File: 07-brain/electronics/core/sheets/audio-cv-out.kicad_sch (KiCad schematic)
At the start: 19 parts, among them U6 MCP6002-xSN, U7 CD4053B, U8 MCP4822

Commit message: Brain schematics WIP
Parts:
- removed C11, C12: 100n, Capacitor_SMD:C_0603_1608Metric, symbol Device:C
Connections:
- net AUDIO_CV_OUT_1: no longer R31.2, R32.2
- net GND renamed GNDA
- net OUT_1_SWITCH renamed OUT_SWITCH_S1
- net OUT_2_SWITCH renamed OUT_SWITCH_S2
- new net AUDIO_CV_OUT_2: R31.2, R32.2
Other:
- note added: "Should I put a resistor on each output of the switch so that the signal can't go back to the switch?"
- moved on the sheet: C13, C14

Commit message: Updated Brain schematics
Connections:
- net OUT_SWITCH_S1 renamed OUT_COUPLING_S1
- net OUT_SWITCH_S2 renamed OUT_COUPLING_S2
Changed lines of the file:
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@@
 		)
 	)
-	(hierarchical_label "OUT_SWITCH_S2"
+	(hierarchical_label "OUT_COUPLING_S2"
 		(shape input)
 		(at 109.22 50.8 180)
@@
 		)
 	)
-	(hierarchical_label "OUT_SWITCH_S1"
+	(hierarchical_label "OUT_COUPLING_S1"
 		(shape input)
 		(at 109.22 48.26 180)

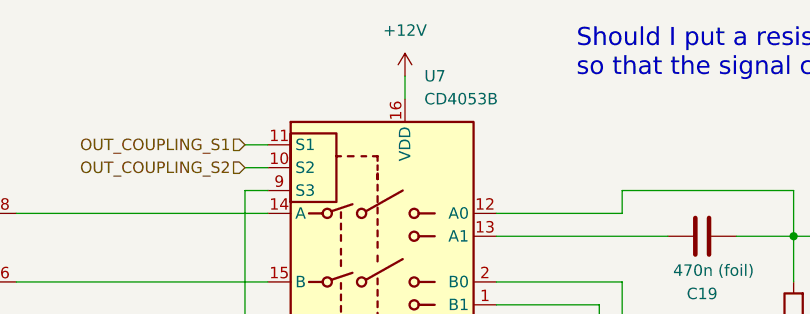
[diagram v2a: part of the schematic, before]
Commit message: Added AudioCVOut class to BrainSDK (untested)
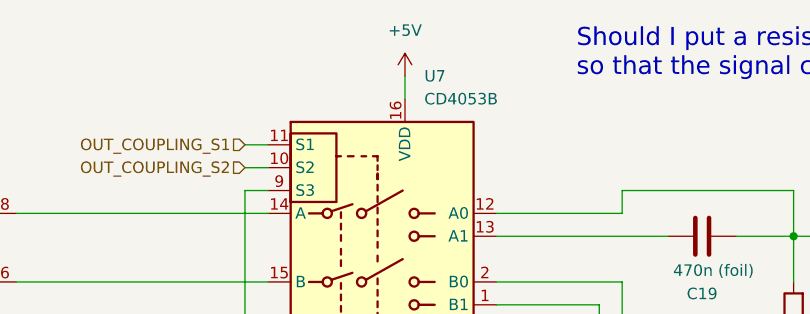
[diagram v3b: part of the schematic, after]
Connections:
- net +12V: no longer U7.16 (VDD)
- net +5V: now also U7.16 (VDD)
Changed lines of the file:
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@@
-	)
-	(symbol
-		(lib_name "+12V_2")
-		(lib_id "power:+12V")
-		(at 127 40.64 0)
-		(unit 1)
-		(exclude_from_sim no)
-		(in_bom yes)
-		(on_board yes)
-		(dnp no)
-		(fields_autoplaced yes)
-		(property "Reference" "#PWR047"
-			(at 127 44.45 0)
-			(effects
-				(font
-					(size 1.27 1.27)
-				)
-				(hide yes)
-			)
-		)
-		(property "Value" "+12V"
-			(at 127 35.56 0)
-			(effects
-				(font
-					(size 1.27 1.27)
-				)
-			)
-		)
-		(property "Footprint" ""
-			(at 127 40.64 0)
-			(effects
-				(font
-					(size 1.27 1.27)
-				)
-				(hide yes)
-			)
-		)
-		(property "Datasheet" ""
-			(at 127 40.64 0)
-			(effects
-				(font
-					(size 1.27 1.27)
-				)
-				(hide yes)
-			)
-		)
-		(property "Description" ""
-			(at 127 40.64 0)
-			(effects
-				(font
-					(size 1.27 1.27)
-				)
-				(hide yes)
-			)
-		)
-		(pin "1"
-		)
-		(instances
-			(project "brain-core"
-				(path "/8e2e31f3-eed5-4de1-966c-f4162758c735/a5dac03c-0548-4574-b19b-4dd5fbd38e47"
-					(reference "#PWR047")
-					(unit 1)
-				)
-			)
-		)
 	)
 	(symbol
@@
 					(unit 1)
 				)
+			)
+		)
+	)
+	(symbol
+		(lib_name "+5V_1")
+		(lib_id "power:+5V")
+		(at 127 40.64 0)
+		(unit 1)
+		(exclude_from_sim no)
+		(in_bom yes)
+		(on_board yes)
+		(dnp no)
+		(fields_autoplaced yes)
+		(property "Reference" "#PWR030"
+			(at 127 44.45 0)
+			(effects
+				(font
+					(size 1.27 1.27)
+				)
+				(hide yes)
+			)
+		)
+		(property "Value" "+5V"
+			(at 127 35.56 0)
+			(effects
+				(font
+					(size 1.27 1.27)
+				)
+			)
+		)
+		(property "Footprint" ""
+			(at 127 40.64 0)
+			(effects
+				(font
+					(size 1.27 1.27)
+				)
+				(hide yes)
+			)
+		)
+		(property "Datasheet" ""
+			(at 127 40.64 0)
+			(effects
+				(font
+					(size 1.27 1.27)
+				)
+				(hide yes)
+			)
+		)
+		(property "Description" "Power symbol creates a global label with name \"+5V\""
+			(at 127 40.64 0)
+			(effects
+				(font
+					(size 1.27 1.27)
+				)
+				(hide yes)
+			)
+		)
+		(pin "1"
+		)
+		(instances
+			(project "brain-core"
+				(path "/8e2e31f3-eed5-4de1-966c-f4162758c735/a5dac03c-0548-4574-b19b-4dd5fbd38e47"
+					(reference "#PWR030")
+					(unit 1)
+				)

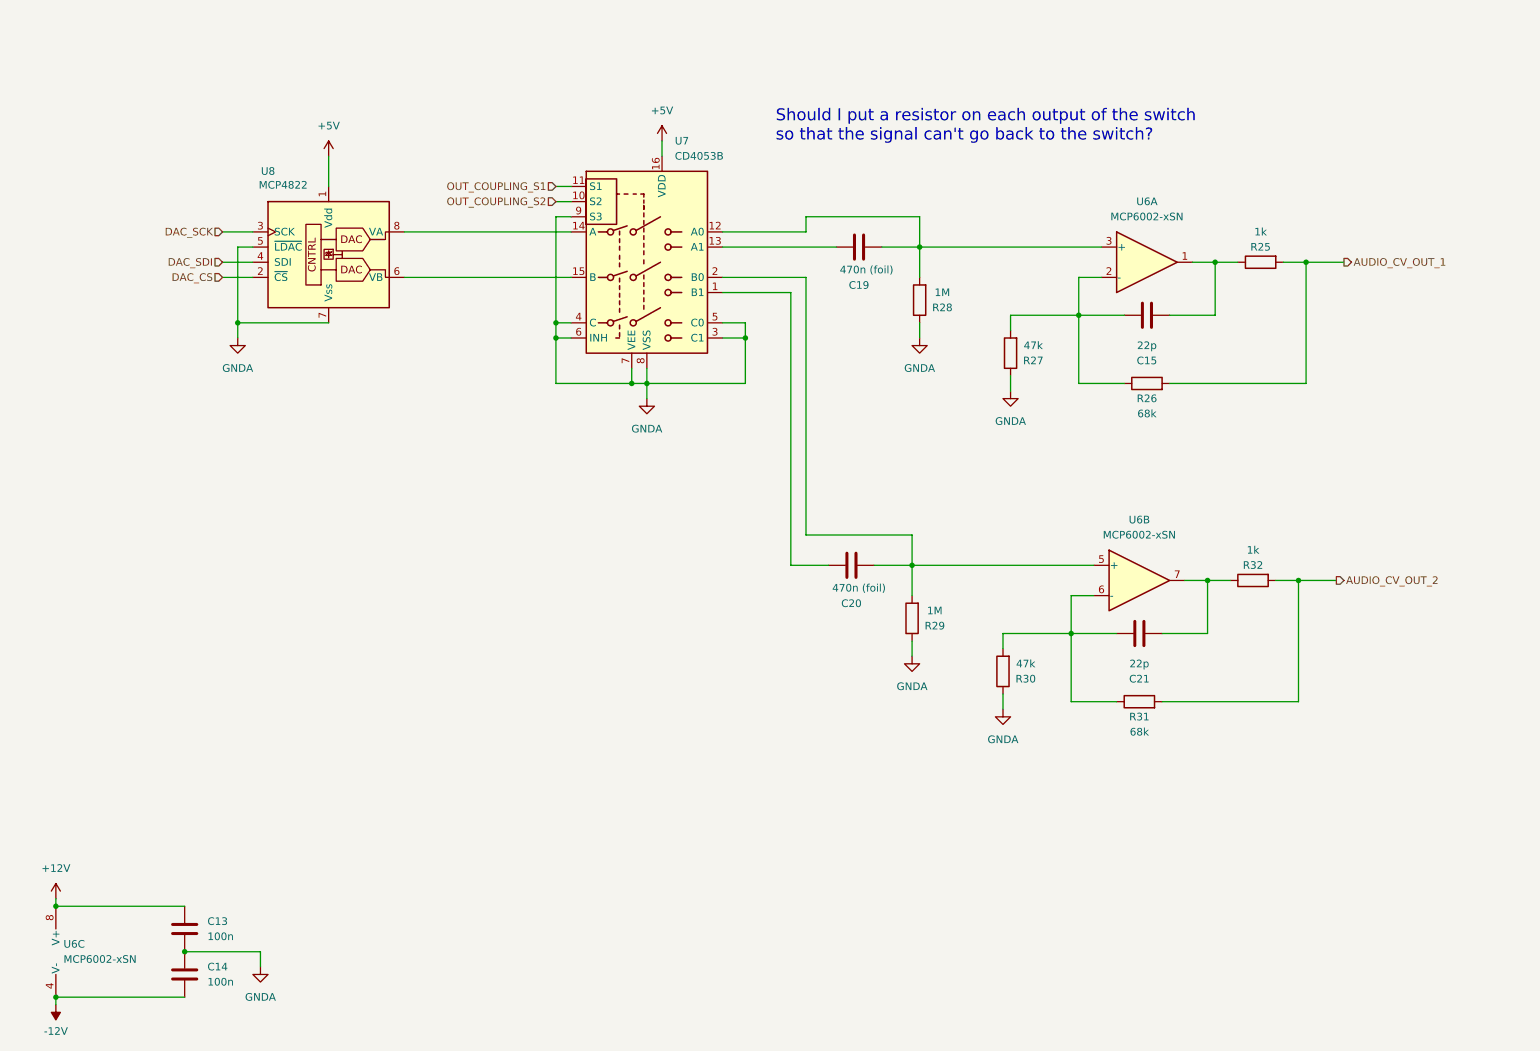
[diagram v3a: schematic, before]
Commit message: Genius level shifter in Brain output
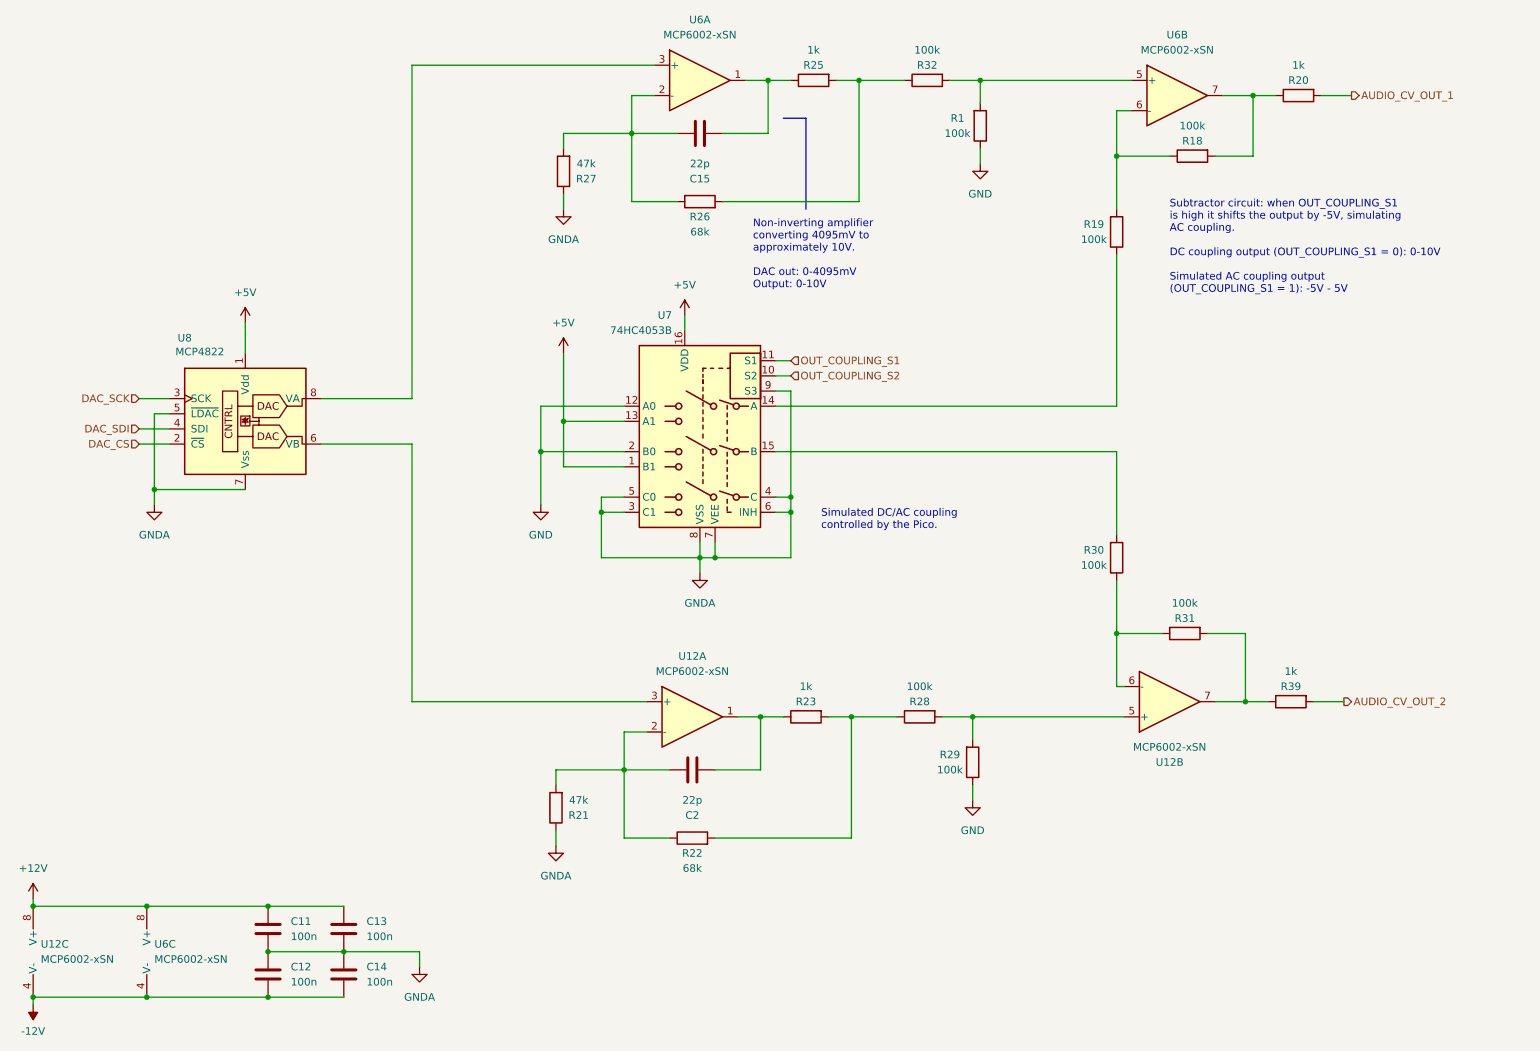
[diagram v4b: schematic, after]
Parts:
- removed C19, C20: 470n (foil), Capacitor_THT:C_Rect_L7.0mm_W3.5mm_P5.00mm, symbol Device:C
- removed C21: 22p, Capacitor_SMD:C_0603_1608Metric, symbol Device:C
- added C11, C12: 100n, Capacitor_SMD:C_0603_1608Metric, symbol Device:C
- added C2: 22p, Capacitor_SMD:C_0603_1608Metric, symbol Device:C
- added R1, R18, R19: 100k, Resistor_SMD:R_0603_1608Metric, symbol Device:R
- added R20, R23, R39: 1k, Resistor_SMD:R_0603_1608Metric, symbol Device:R
- added R21: 47k, Resistor_SMD:R_0603_1608Metric, symbol Device:R
- added R22: 68k, Resistor_SMD:R_0603_1608Metric, symbol Device:R
- added U12: MCP6002-xSN, symbol Amplifier_Operational:MCP6002-xSN
- R28, R29: value 1M -> 100k
- R30: value 47k -> 100k
- R31: value 68k -> 100k
- R32: value 1k -> 100k
- U7: value CD4053B -> 74HC4053B
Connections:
- net +12V: now also C11.1, U12.8 (V+)
- net +5V: now also U7.1 (B1), U7.13 (A1)
- net -12V: now also C12.2, U12.4 (V-)
- net AUDIO_CV_OUT_1: now also R20.2; no longer R25.2, R26.2
- net AUDIO_CV_OUT_2: now also R39.2; no longer R31.2, R32.2
- net GNDA: now also C11.2, C12.1, R21.1; no longer R28.1, R29.1, R30.1
- net at R32.1: now also R25.2, R26.2; no longer U6.7
- net at U8.6 (VB): now also U12.3 (+); no longer U7.15 (B)
- net at U7.14 (A): now also R19.1; no longer U8.8 (VA)
- new net: R18.1, R19.2, U6.6 (-)
- new net: R28.2, R29.2, U12.5 (+)
- new net: R1.2, R32.2, U6.5 (+)
- new net: U6.3 (+), U8.8 (VA)
- new net: C2.2, R23.1, U12.1
- new net: R22.2, R23.2, R28.1
- new net: R31.2, R39.1, U12.7
- new net: C2.1, R21.2, R22.1, U12.2 (-)
- new net: R30.1, R31.1, U12.6 (-)
- new net: R30.2, U7.15 (B)
- new net: R18.2, R20.1, U6.7
- new net GND: R1.1, R29.1, U7.12 (A0), U7.2 (B0)
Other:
- note added: "Non-inverting amplifier converting 4095mV to approximately 10V. DAC out: 0-4095mV Output: 0-10V"
- note added: "Simulated DC/AC coupling controlled by the Pico."
- note added: "Subtractor circuit: when OUT_COUPLING_S1 is high it shifts the output by -5V, simulating AC coupling. DC coupling output (OUT_COUPLING_S1 = 0): 0-10V Simulated AC coupling output (OUT_COUPLING_S1 = 1): -5V - 5V"
- note removed: "Should I put a resistor on each output of the switch so that the signal can't go back to the switch?"
- moved on the sheet: C13, C14, C15, R25, R26, R27, R32, U6A, U6B, U6C, U7, U8

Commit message: Audio/CV out BrainSDK tested/working
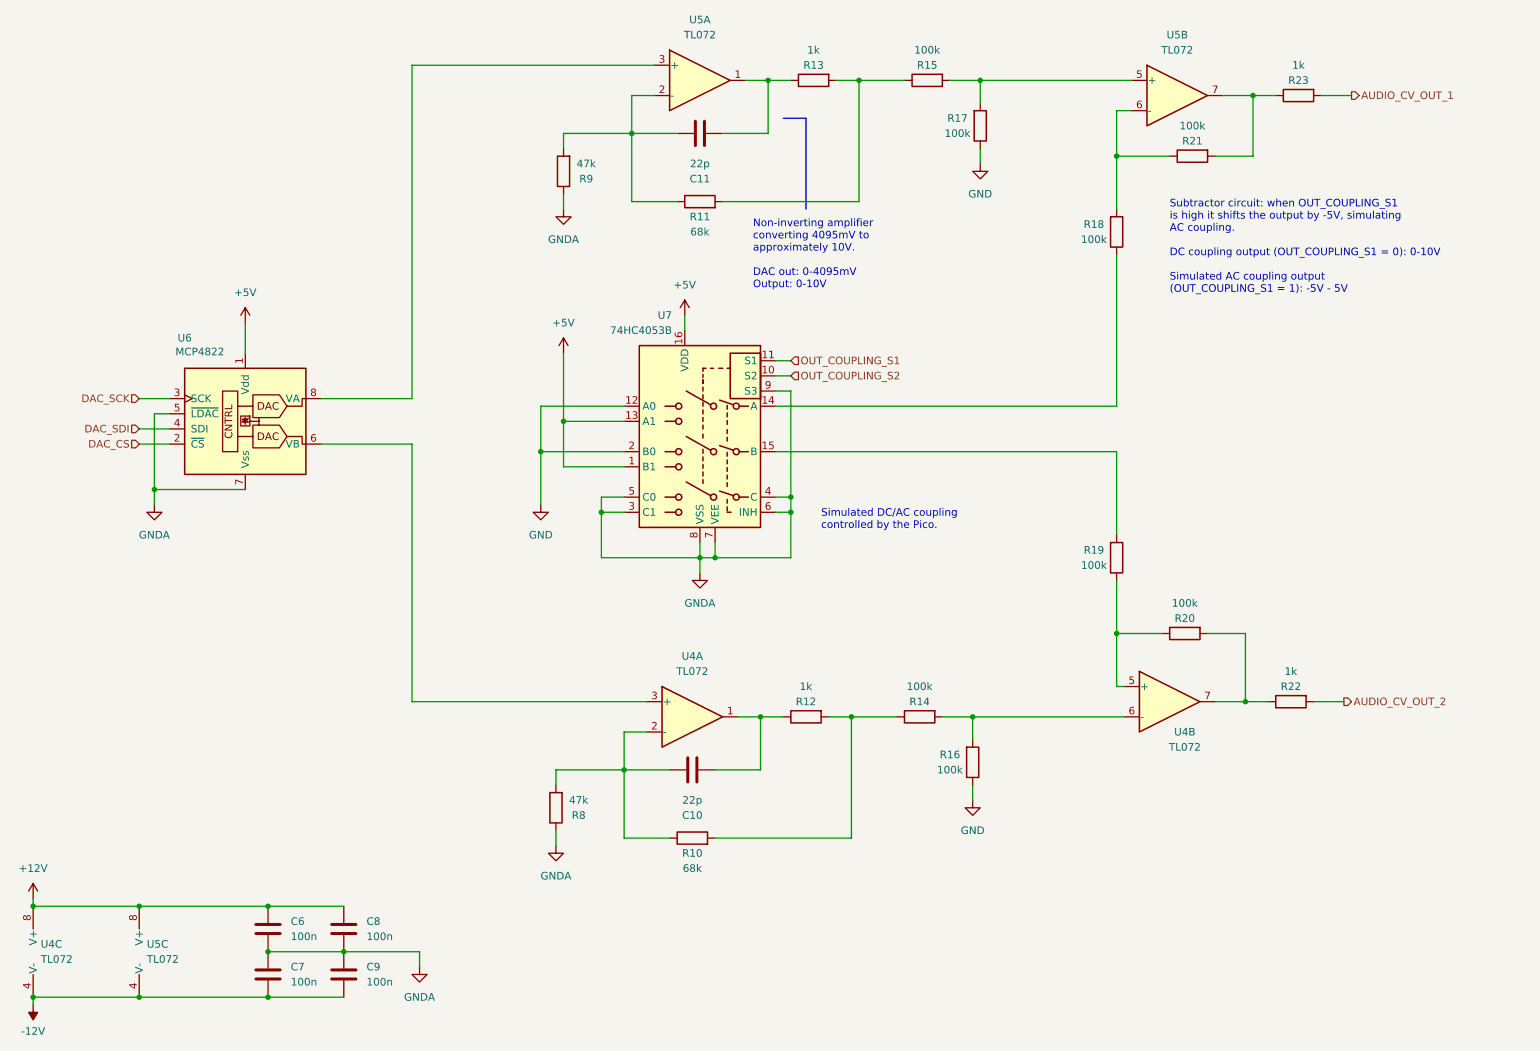
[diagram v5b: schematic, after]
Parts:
- removed U12, U6: MCP6002-xSN, symbol Amplifier_Operational:MCP6002-xSN
- added U4, U5: TL072, symbol Amplifier_Operational:TL072
- renumbered C2 to C10, C15 to C11, C11 to C6, C12 to C7, C13 to C8, C14 to C9, R22 to R10, R26 to R11, R23 to R12, R25 to R13, R28 to R14, R32 to R15, R29 to R16, R1 to R17, R19 to R18, R30 to R19, R31 to R20, R18 to R21, R39 to R22, R20 to R23, R21 to R8, R27 to R9, U8 to U6
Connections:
- net +12V: now also U4.8 (V+), U5.8 (V+)
- net -12V: now also U4.4 (V-), U5.4 (V-)
- net at R18.2, R21.1: now also U5.6 (-)
- net at R14.2, R16.2: now also U4.6 (-)
- net at R15.2, R17.2: now also U5.5 (+)
- net at U6.6 (VB): now also U4.3 (+)
- net at U6.8 (VA): now also U5.3 (+)
- net at C11.1, R11.1, R9.2: now also U5.2 (-)
- net at C10.2, R12.1: now also U4.1
- net at R20.2, R22.1: now also U4.7
- net at C11.2, R13.1: now also U5.1
- net at C10.1, R10.1, R8.2: now also U4.2 (-)
- net at R19.1, R20.1: now also U4.5 (+)
- net at R21.2, R23.1: now also U5.7
